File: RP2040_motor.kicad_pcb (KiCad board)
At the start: 4 copper layers, 85.5 x 54 mm, 173 parts, among them J1 USB_C_Receptacle_USB2.0, J2 Conn_01x05, J3 Conn_01x06, J4 Conn_01x04, J5 Conn_01x04, J6 Conn_01x03, SW1 SW_MEC_5G, U1 EG2131, U10 EG2131, U11 RP2040, U12 EG2131, U13 ADC081S021CISD/NOPB, U2 EG2131, U3 LM358, U4 EG2131, U5 EG2131, U6 NCP1117-3.3_SOT223, U7 XL7045, U8 LM358, U9 W25Q128JVS, Y1 Crystal_GND24

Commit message: I think layout is complete and the board is ready to order.
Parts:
- added D34: WS2812B, RP2040_minimal:LED_WS2812_3528_3.5x2.8mm_P1.5mm, F.Cu at (108.4, 70.1)
- added D35: WS2812B, RP2040_minimal:LED_WS2812_3528_3.5x2.8mm_P1.5mm, F.Cu at (111.8, 70.1)
- added D36: WS2812B, RP2040_minimal:LED_WS2812_3528_3.5x2.8mm_P1.5mm, F.Cu at (115.2, 70.1)
- added G***: LOGO, taylor_footprints:twisted_2, B.Cu at (137.5, 86.3)
- added G***: LOGO, taylor_footprints:twisted_icon, B.Cu at (115.7, 86.0)
- added G***: LOGO, taylor_footprints:twisted, B.Cu at (128.7, 82.8)
- added JP1: SolderJumper_2_Open, Jumper:SolderJumper-2_P1.3mm_Open_RoundedPad1.0x1.5mm, F.Cu at (105.2, 75.0)
- moved D24 11.6 mm to (105.3, 70.4), turned to -90 degrees
- moved C18 6.48 mm to (114.6, 80.5)
- moved D28 6.44 mm to (109.4, 74.3)
- moved U12 5.17 mm to (114.2, 76.6)
- moved D27 4.98 mm to (107.6, 77.7)
- moved R56 4.90 mm to (109.5, 77.7)
- moved R57 3.67 mm to (107.6, 74.4)
- moved C28 3.32 mm to (110.8, 80.4), turned to 180 degrees
- moved D29 2.18 mm to (135.7, 97.2)
- moved U5 2.11 mm to (112.6, 84.4)
- moved C24 2.04 mm to (113.7, 73.0), turned to 180 degrees
- moved R26 2.02 mm to (107.9, 81.6)
- moved D16 1.63 mm to (106.0, 81.0)
- moved D9 1.62 mm to (135.3, 91.8)
- moved R58 1.45 mm to (144.5, 93.3)
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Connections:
- R13 pad 1: VSENSE2B -> VSENSE2C
- R28 pad 1: VSENSE1A -> VSENSE1B
- R37 pad 1: VSENSE2C -> VSENSE2B
- R7 pad 1: VSENSE1B -> VSENSE1A
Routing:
- net SPI0TX: track 17.7 -> 67.3 mm, vias 1 -> 3
- net +3V3: track 99.1 -> 140.0 mm, vias 3 -> 9
- net Net-(BL2-Pad2): track 53.8 -> 45.9 mm
- net Net-(BL1-Pad2): track 50.8 -> 58.6 mm
- net Net-(D34-Pad4): track 0.00 -> 7.74 mm, vias 0 -> 2
- net Net-(D35-Pad4): track 0.00 -> 7.68 mm, vias 0 -> 2
- net Net-(C18-Pad2): track 11.4 -> 17.3 mm, vias 0 -> 2
- net +12V: track 213.7 -> 219.5 mm, vias 9 -> 10
- net Net-(C28-Pad2): track 12.1 -> 17.7 mm, vias 0 -> 2
- net Net-(D34-Pad2): track 0.00 -> 5.41 mm
- net M1B: track 42.4 -> 47.1 mm, vias 35 -> 33
- net GND: track 74.7 -> 78.6 mm, vias 225 -> 202
- net VSENSE1B: track 22.6 -> 19.1 mm, vias 2 -> 0
- net A4: track 78.8 -> 82.0 mm, vias 6 -> 4
- net M2C: track 38.7 -> 41.8 mm, vias 34 -> 31
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- added copper zone on B.Cu, net M1A
- added copper zone on B.Cu, net M1B
- added copper zone on B.Cu, net M1C
- added copper zone on B.Cu, net M2A
- added copper zone on B.Cu, net M2B
- added copper zone on B.Cu, net M2C
- added copper zone on B.Cu, net VMOT
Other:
- board text added: "A1"
- board text added: "A2"
- board text added: "B1"
- board text added: "B2"
- board text added: "BOOT"
- board text added: "C1"
- board text added: "C2"
- board text added: "Designed by Taylor Alexander For Twisted Fields"
- board text added: "ENC2"
- board text added: "Funded By Daniel Theobald Thanks Daniel!"
- board text added: "I2C"
- board text added: "Please clone this board!"
- board text added: "RP2040 Brushless Motor Controller"
- board text added: "SPI/ENC1"
- board text added: "Serial"
- board text added: "The smallest change can be the beginning of something big."
- board text added: "VMOT"
- board text added: "Version 1"
- board text added: "We are all star stuff."
- board text added: "We need your help. Fork the design and make it yours."
- board text added: "You can do it!"
- board text added: "github.com/Twisted-Fields/rp2040-motor-controller"
- board text removed: "3V3"
- board text removed: "GP0"
- board text removed: "GP1"
- board text removed: "GP10"
- board text removed: "GP11"
- board text removed: "GP12"
- board text removed: "GP13"
- board text removed: "GP14"
- board text removed: "GP15"
- board text removed: "GP2"
- board text removed: "GP3"
- board text removed: "GP4"
- board text removed: "GP5"
- board text removed: "GP6"
- board text removed: "GP7"
- board text removed: "GP8"
- board text removed: "GP9"
- board text removed: "Outer Row GND"
- board text removed: "USB_BOOT"

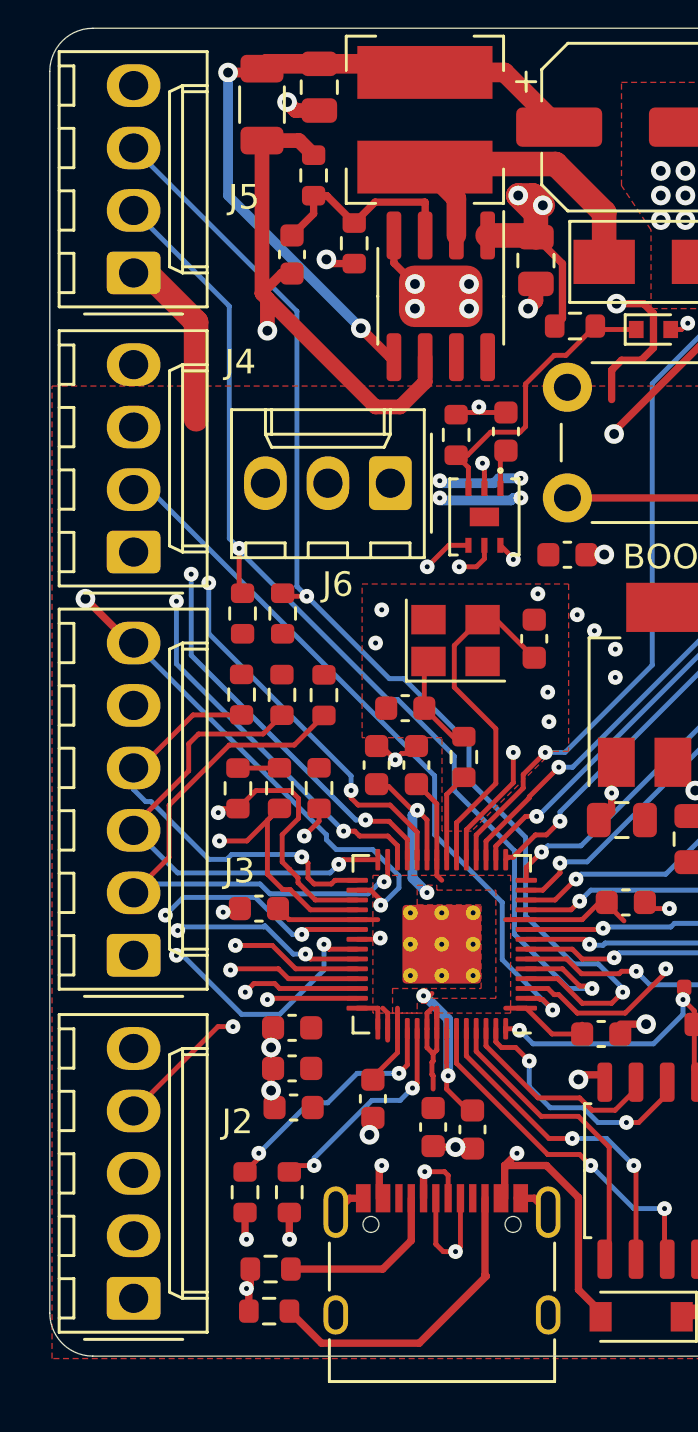
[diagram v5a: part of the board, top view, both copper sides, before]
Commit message: Small updates to copper and silk
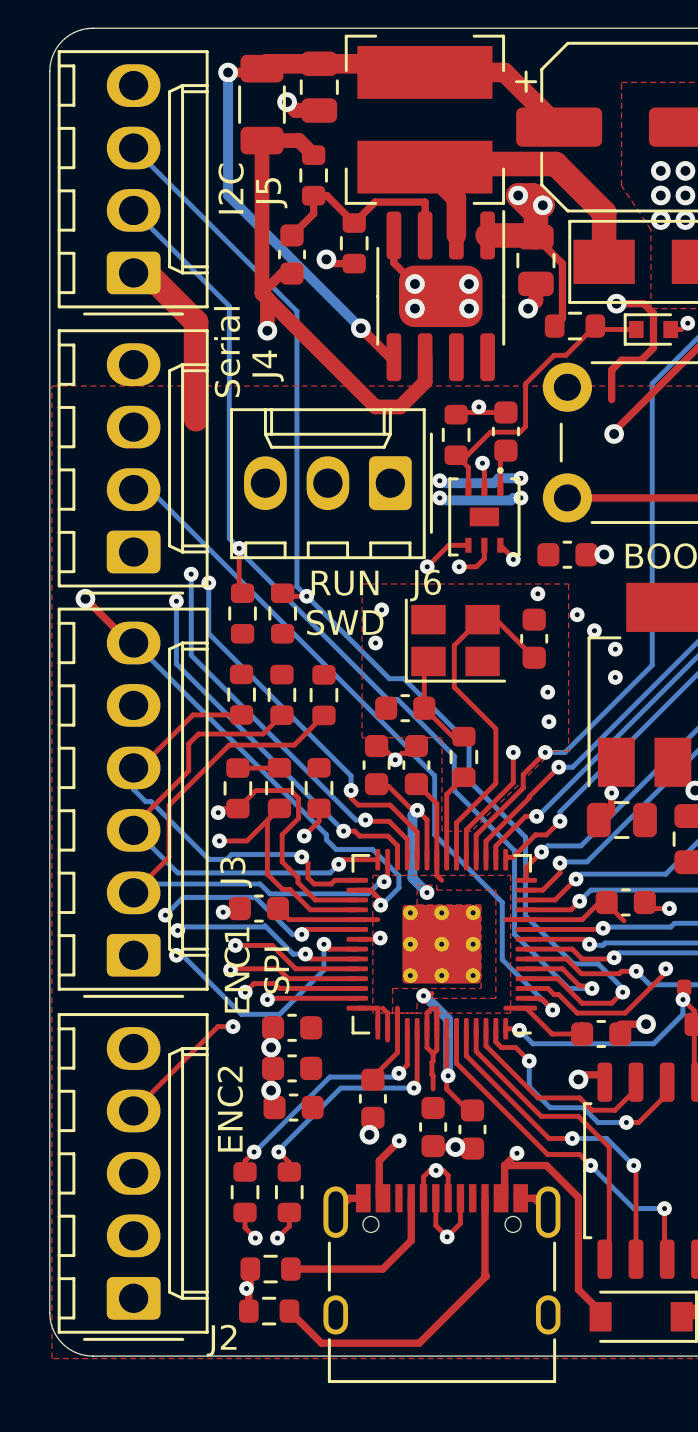
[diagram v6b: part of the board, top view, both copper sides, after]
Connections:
- net Net-(R47-Pad2) renamed /power_and_cpu/USB_DP
- net Net-(R48-Pad2) renamed /power_and_cpu/USB_DN
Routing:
- net /power_and_cpu/USB_D+: track 13.5 -> 15.2 mm
- net /power_and_cpu/USB_DP: track 9.09 -> 10.2 mm
- net /power_and_cpu/USB_D-: track 15.4 -> 14.6 mm
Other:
- board text added: "ENC1 SPI"
- board text added: "RUN SWD"
